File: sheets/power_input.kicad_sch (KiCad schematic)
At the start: 0 parts

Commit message: sch: power input (CH224K PD + 802.3at PoE flyback + 12V OR)
Co-Authored-By: Claude Fable 5 <noreply@anthropic.com>
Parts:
- added BR1, BR2: MB10S, Diode_SMD:D_MBS-4, symbol sierra-to-usb:MB10S
- added C32: 1µF/25V, C_0603, symbol Device:C_Small
- added C_BULK: 68µF/100V, CP_Elec_8x10.5, symbol Device:C_Small
- added C_CLAMP: 0.047µF/250V, C_1206, symbol Device:C_Small
- added C_COMPz: 3.9nF, C_0603, symbol Device:C_Small
- added C_CSF: 100pF, C_0603, symbol Device:C_Small
- added C_GAT2: 0.22µF, C_0603, symbol Device:C_Small
- added C_OUT1: 560µF/25V, CP_Elec_10x10.5, symbol Device:C_Small
- added C_OUT2: 22µF/35V, C_1210, symbol Device:C_Small
- added C_SHIELD: 1nF, C_0603, symbol Device:C_Small
- added C_SST: 47nF, C_0603, symbol Device:C_Small
- added C_VB, C_VBG: 0.1µF, C_0603, symbol Device:C_Small
- added C_VDD: 1µF, C_0603, symbol Device:C_Small
- added D12, D13: MBRS340, Diode_SMD:D_SMC, symbol Device:D_Small
- added D16: MMSD914T1G, D_SOD-123, symbol Device:D_Small
- added D17: MMSZ4685T1G (15V), D_SOD-123, symbol Device:D_Zener_Small
- added D6: SMAJ13A, Diode_SMB:D_SMB, symbol Diode:SMAJ13A
- added D7: SMAJ58A, Diode_SMB:D_SMB, symbol Diode:SMAJ58A
- added D8: BAT54, D_SOD-123, symbol Device:D_Small
- added D9: MMSZ5245B (15V), D_SOD-123, symbol Device:D_Zener_Small
- added J2: TYPE-C-31-M-12, symbol Connector:USB_C_Receptacle_USB2.0_16P
- added L1: 15µH, L_12x12, symbol Device:L
- added L9: 2.2mH, L_0805, symbol Device:L
- added Q20: FDMS86250, Package_TO_SOT_SMD:PQFN-8, symbol Device:Q_NMOS
- added Q21: FDMC2523P, Package_DFN_QFN:QFN-8_2x2mm_P0.5mm, symbol Device:Q_PMOS
- added Q30, Q31: IRLR7843TRPBF, Package_TO_SOT_SMD:TO-252-2, symbol Device:Q_NMOS
- added R41: 2.00kΩ, R_0603, symbol Device:R_Small
- added R45: 40.2kΩ, R_0603, symbol Device:R_Small
- added R53: 10.5kΩ, R_0603, symbol Device:R_Small
- added R_BTPULL, R_GAT2, R_PGPULL, R_VBUSSENSE: 10kΩ, R_0603, symbol Device:R_Small
- added R_CFG1: 24kΩ, R_0603, symbol Device:R_Small
- added R_CLSA, R_CLSB: 32Ω, R_0603, symbol Device:R_Small
- added R_COMPz: 1.00kΩ, R_0603, symbol Device:R_Small
- added R_CS: 0.05Ω, R_2512, symbol Device:R_Small
- added R_CSF, R_VDD: 1kΩ, R_0603, symbol Device:R_Small
- added R_DEN: 25.5kΩ, R_0603, symbol Device:R_Small
- added R_DT: 42.2kΩ, R_0603, symbol Device:R_Small
- added R_FRS: 60.4kΩ, R_0603, symbol Device:R_Small
- added R_G1: 10Ω, R_0603, symbol Device:R_Small
- added R_ISTP: 499kΩ, R_0603, symbol Device:R_Small
- added R_LINEUV_HI: 110kΩ, R_0603, symbol Device:R_Small
- added R_LINEUV_LO: 10.0kΩ, R_0603, symbol Device:R_Small
- added R_REF: 49.9kΩ, R_0603, symbol Device:R_Small
- added R_SHIELD: 1MΩ, R_0603, symbol Device:R_Small
- added T1: WE 750313355, Transformer_SMT_XFRMR_29MM08_23MM1, symbol sierra-to-usb:WE750313355
- added U10: TPS23730RMTR, Package_DFN_QFN:QFN-45-1EP_7x5mm_P0.4mm_EP3.6x3.4mm, symbol sierra-to-usb:TPS23730
- added U19, U21: LM5050MKX-1/NOPB, Package_TO_SOT_SMD:SOT-23-6, symbol sierra-to-usb:LM5050-1
- added U2: CH224K, Package_SO:SSOP-10-1EP_3.9x4.9mm_P1mm_EP2.1x3.3mm, symbol Interface_USB:CH224K
- added U20: TCMT1107, Package_SO:SOP-4_4.4x2.6mm_P1.27mm, symbol Isolator:TCMT1107
- added U22: TL431IDBVR, Package_TO_SOT_SMD:SOT-23-5, symbol Reference_Voltage:TL431DBV
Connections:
- new net +12V: Q30.D, Q31.D, U19.1 (VS), U19.6 (OUT), U21.1 (VS), U21.6 (OUT)
- new net +12V_POE: C_OUT1.1, C_OUT2.1, L1.2, Q31.S, R41.1, R45.1, U21.4 (IN)
- new net +3V3: R_BTPULL.2, R_PGPULL.2
- new net CH224K_CFG1: R_CFG1.1, U2.9 (CFG1)
- new net CH224K_PG: R_PGPULL.1, U2.10 (PG)
- new net CS_SENSE: Q20.S, R_CS.1, R_CSF.1
- new net GND: C_OUT1.2, C_OUT2.2, C_SHIELD.2, C_VDD.2, D13.1 (K), D6.2 (A2), J2.A1 (GND), J2.A12 (GND), J2.B1 (GND), J2.B12 (GND), R53.2, R_CFG1.2, R_SHIELD.2, T1.10 (N2.2), T1.11 (N2.2), T1.12 (N2.2), U19.2 (GND), U19.3 (OFF), U2.11 (GND), U21.2 (GND), U21.3 (OFF), U22.5 (A)
- new net N_ACDRV: C_GAT2.2, D9.2 (A), R_GAT2.1
- new net N_ACLAMP_D: C_CLAMP.1, Q21.D
- new net N_ACLAMP_G: Q21.G, R_GAT2.2
- new net N_BIAS_L_IN: L9.1, T1.5 (N3.1)
- new net N_BIAS_RECT_IN: D16.2 (A), L9.2
- new net N_CH224K_VBUSSENSE: R_VBUSSENSE.2, U2.8 (VBUS)
- new net N_CH224K_VDD: C_VDD.1, R_VDD.2, U2.1 (VDD)
- new net N_FBTAP: R45.2, R53.1, U22.4 (REF)
- new net N_G1: D8.2 (A), Q20.G, R_G1.2
- new net N_GAT2: C_GAT2.1, U10.41 (GAT2)
- new net N_GATE: D8.1 (K), R_G1.1, U10.43 (GATE)
- new net N_J2_SHIELD: C_SHIELD.1, J2.SH (SHIELD), R_SHIELD.1
- new net N_LED_A: R41.2, U20.1
- new net N_OPTO_E: R_COMPz.1, U20.3
- new net N_SEC_PLUS: D12.1 (K), T1.7 (N2.1), T1.8 (N2.1), T1.9 (N2.1)
- new net N_TL_K: U20.2, U22.3 (K)
- new net N_U10_CLSA: R_CLSA.1, U10.21 (CLSA)
- new net N_U10_CLSB: R_CLSB.1, U10.20 (CLSB)
- new net N_U10_COMP: C_COMPz.1, R_COMPz.2, U10.35 (COMP)
- new net N_U10_CS: C_CSF.1, R_CSF.2, U10.1 (CS)
- new net N_U10_DEN: R_DEN.1, U10.24 (DEN)
- new net N_U10_DT: R_DT.1, U10.31 (DT)
- new net N_U10_FRS: R_FRS.1, U10.4 (FRS)
- new net N_U10_ISTP: R_ISTP.1, U10.32 (I_STP)
- new net N_U10_LINEUV: R_LINEUV_HI.2, R_LINEUV_LO.1, U10.38 (LINEUV)
- new net N_U10_REF: R_REF.1, U10.17 (REF)
- new net N_U10_SST: C_SST.1, U10.33 (SST)
- new net N_U10_VB: C_VB.1, U10.3 (DTHR), U10.34 (FB), U10.37 (VB), U20.4
- new net N_U10_VBG: C_VBG.1, U10.40 (VBG)
- new net N_U10_VCC: C32.1, D16.1 (K), D17.1 (K), U10.42 (VCC)
- new net N_U19_GATE: Q30.G, U19.5 (GATE)
- new net N_U21_GATE: Q31.G, U21.5 (GATE)
- new net PD_CC1: J2.A5 (CC1), U2.7 (CC1)
- new net PD_CC2: J2.B5 (CC2), U2.6 (CC2)
- new net POE_RTN: BR1.3 (-), BR2.3 (-), C32.2, C_BULK.2, C_COMPz.2, C_CSF.2, C_SST.2, C_VB.2, C_VBG.2, D17.2 (A), D7.2 (A2), R_CLSA.2, R_CLSB.2, R_CS.2, R_DT.2, R_FRS.2, R_ISTP.2, R_LINEUV_LO.2, R_REF.2, T1.6 (N3.2), U10.11 (EMPS), U10.18 (SCDIS), U10.19 (PPD), U10.2 (AGND), U10.27 (VSS1), U10.28 (VSS2), U10.39 (PSRS), U10.44 (CP), U10.45 (GND), U10.46 (PAD_G), U10.47 (PAD_S), U10.5 (APD), U10.7 (RTN1), U10.8 (RTN2), U10.9 (RTN3)
- new net POE_STATUS: R_BTPULL.1, U10.12 (BT)
- new net POE_VA+: BR1.2
- new net POE_VA-: BR1.4
- new net POE_VB+: BR2.2
- new net POE_VB-: BR2.4
- new net POE_VDD54: BR1.1 (+), BR2.1 (+), C_BULK.1, D7.1 (A1), D9.1 (K), Q21.S, R_DEN.2, R_LINEUV_HI.1, T1.1 (N1.1), T1.2 (N1.1), U10.23 (VDD)
- new net SW2: D12.2 (A), D13.2 (A), L1.1
- new net SW_NODE: C_CLAMP.2, Q20.D, T1.3 (N1.2), T1.4 (N1.2)
- new net VBUS_PD: D6.1 (A1), J2.A4 (VBUS), J2.A9 (VBUS), J2.B4 (VBUS), J2.B9 (VBUS), Q30.S, R_VBUSSENSE.1, R_VDD.1, U19.4 (IN)
- no-connect marks 0 -> 22

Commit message: sch: power_input rework — faithful EVM-093 transcription, VSS/RTN split, sync rect, opto/comp per EVM
Co-Authored-By: Claude Fable 5 <noreply@anthropic.com>
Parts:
- removed C_BULK: 68µF/100V, CP_Elec_8x10.5, symbol Device:C_Small
- removed C_CLAMP: 0.047µF/250V, C_1206, symbol Device:C_Small
- removed C_COMPz: 3.9nF, C_0603, symbol Device:C_Small
- removed C_CSF: 100pF, C_0603, symbol Device:C_Small
- removed C_GAT2: 0.22µF, C_0603, symbol Device:C_Small
- removed C_OUT1: 560µF/25V, CP_Elec_10x10.5, symbol Device:C_Small
- removed C_OUT2: 22µF/35V, C_1210, symbol Device:C_Small
- removed C_SHIELD: 1nF, C_0603, symbol Device:C_Small
- removed C_SST: 47nF, C_0603, symbol Device:C_Small
- removed C_VB, C_VBG: 0.1µF, C_0603, symbol Device:C_Small
- removed C_VDD: 1µF, C_0603, symbol Device:C_Small
- removed D16: MMSD914T1G, D_SOD-123, symbol Device:D_Small
- removed D17: MMSZ4685T1G (15V), D_SOD-123, symbol Device:D_Zener_Small
- removed D6: SMAJ13A, Diode_SMB:D_SMB, symbol Diode:SMAJ13A
- removed D7: SMAJ58A, Diode_SMB:D_SMB, symbol Diode:SMAJ58A
- removed L9: 2.2mH, L_0805, symbol Device:L
- removed R41: 2.00kΩ, R_0603, symbol Device:R_Small
- removed R45: 40.2kΩ, R_0603, symbol Device:R_Small
- removed R53: 10.5kΩ, R_0603, symbol Device:R_Small
- removed R_BTPULL, R_GAT2, R_PGPULL, R_VBUSSENSE: 10kΩ, R_0603, symbol Device:R_Small
- removed R_CFG1: 24kΩ, R_0603, symbol Device:R_Small
- removed R_CLSA, R_CLSB: 32Ω, R_0603, symbol Device:R_Small
- removed R_COMPz: 1.00kΩ, R_0603, symbol Device:R_Small
- removed R_CS: 0.05Ω, R_2512, symbol Device:R_Small
- removed R_CSF, R_VDD: 1kΩ, R_0603, symbol Device:R_Small
- removed R_DEN: 25.5kΩ, R_0603, symbol Device:R_Small
- removed R_DT: 42.2kΩ, R_0603, symbol Device:R_Small
- removed R_FRS: 60.4kΩ, R_0603, symbol Device:R_Small
- removed R_G1: 10Ω, R_0603, symbol Device:R_Small
- removed R_ISTP: 499kΩ, R_0603, symbol Device:R_Small
- removed R_LINEUV_HI: 110kΩ, R_0603, symbol Device:R_Small
- removed R_LINEUV_LO: 10.0kΩ, R_0603, symbol Device:R_Small
- removed R_REF: 49.9kΩ, R_0603, symbol Device:R_Small
- removed R_SHIELD: 1MΩ, R_0603, symbol Device:R_Small
- added C1: 1uF, C_0603, symbol Device:C_Small
- added C10: 470pF/100V, C_0805, symbol Device:C_Small
- added C11: 2.2nF/50V, C_0603, symbol Device:C_Small
- added C12: 47nF/50V, C_0603, symbol Device:C_Small
- added C13, C14: 0.1uF/25V, C_0603, symbol Device:C_Small
- added C15: 0.1uF/50V, C_0805, symbol Device:C_Small
- added C16: 1uF/25V, C_0805, symbol Device:C_Small
- added C17: 0.047uF/250V, C_1206, symbol Device:C_Small
- added C18: 0.22uF/50V, C_0805, symbol Device:C_Small
- added C19: 2200pF/2kV, C_1808, symbol Device:C_Small
- added C2: 1nF, C_0603, symbol Device:C_Small
- added C20: 1nF/100V, C_0603, symbol Device:C_Small
- added C21, C23: 0.047uF/100V, C_1206, symbol Device:C_Small
- added C22, C31: 100pF/25V, C_0603, symbol Device:C_Small
- added C24: 1000pF/100V, C_1206, symbol Device:C_Small
- added C25: 39uF/16V, CP_Elec_6.3x5.8, symbol Device:C_Small
- added C26, C27: 22uF/35V, C_1210, symbol Device:C_Small
- added C28: 560uF/25V, CP_Elec_10x10.5, symbol Device:C_Small
- added C29: 68nF/16V, C_0603, symbol Device:C_Small
- added C3, C9: 0.1uF/100V, C_1206, symbol Device:C_Small
- added C30: 1uF/50V, C_0805, symbol Device:C_Small
- added C4: 68uF/100V, CP_Elec_10x13, symbol Device:C_Small
- added C5, C6, C7: 2.2uF/100V, C_1210, symbol Device:C_Small
- added C8: 0.1uF/100V, C_0805, symbol Device:C_Small
- added D1, D2, D3, D4, D5: MMSD914T1G, D_SOD-123, symbol Device:D_Small
- added D14: MMSZ5242B-7-F 12V, D_SOD-123, symbol Device:D_Zener_Small
- added D15: BAT54S-7-F, Package_TO_SOT_SMD:SOT-23, symbol Diode:BAT54S
- added D16: Yellow 0603, LED_0603, symbol Device:LED
- added D6: SMAJ13A, Diode_SMB:D_SMB, symbol sierra-to-usb:SMAJ13A
- added D7: SMAJ58A, Diode_SMB:D_SMB, symbol sierra-to-usb:SMAJ58A
- added L2: 5.5uH, L_WE-HC6, symbol Device:L
- added L3: 2.2mH, L_7x7, symbol Device:L
- added Q22, Q23: BSC057N08NS3 G, Package_TO_SOT_SMD:PG-TDSON-8, symbol Device:Q_NMOS
- added Q24, Q25: FCX493TA, Package_TO_SOT_SMD:SOT-89-3, symbol Device:Q_NPN
- added R1: 1k, R_0603, symbol Device:R_Small
- added R10: 110k, R_0603, symbol Device:R_Small
- added R11, R18, R33, R37, R38: 10.0k, R_0603, symbol Device:R_Small
- added R12: 237k, R_0603, symbol Device:R_Small
- added R13: 60.4k, R_0603, symbol Device:R_Small
- added R14: 49.9k, R_0603, symbol Device:R_Small
- added R15: 42.2k, R_0603, symbol Device:R_Small
- added R16: 499k, R_0603, symbol Device:R_Small
- added R17: 10.0, R_0603, symbol Device:R_Small
- added R19: 3.00k, R_0603, symbol Device:R_Small
- added R2, R4: 10k, R_0603, symbol Device:R_Small
- added R20: 0.05/1W, R_1206, symbol Device:R_Small
- added R21: 4.02k, R_1206, symbol Device:R_Small
- added R22: 8.06k, R_1206, symbol Device:R_Small
- added R23: 2.0k, R_0603, symbol Device:R_Small
- added R24: 5.10, R_0805, symbol Device:R_Small
- added R25, R26: 10k/1W, R_2512, symbol Device:R_Small
- added R27: 100/1W, R_2512, symbol Device:R_Small
- added R28: 49.9, R_0603, symbol Device:R_Small
- added R29: 40.2k, R_0603, symbol Device:R_Small
- added R3: 24k, R_0603, symbol Device:R_Small
- added R30: 10.5k, R_0603, symbol Device:R_Small
- added R31, R32, R35: 2.00k, R_0603, symbol Device:R_Small
- added R34, R36: 1.00k, R_0603, symbol Device:R_Small
- added R5: 1M, R_0603, symbol Device:R_Small
- added R6: 25.5k, R_0603, symbol Device:R_Small
- added R7, R8: 32, R_0805, symbol Device:R_Small
- added R9: 15.0k, R_0603, symbol Device:R_Small
- added U23: FOD817DS, Package_DIP:DIP-4_W7.62mm_SMDGullWing, symbol Isolator:PC817
- C32: value 1µF/25V -> 3.9nF/50V
- D12, D13: value MBRS340 -> MURA110T3G; footprint Diode_SMD:D_SMC -> D_SMA
- D8: value BAT54 -> MMSD914T1G
- D9: value MMSZ5245B (15V) -> MMSZ5242B-7-F 12V
- L1: value 15µH -> 15uH; footprint L_12x12 -> L_18x18
- Q20: footprint Package_TO_SOT_SMD:PQFN-8 -> Package_DFN_QFN:PQFN08A
- Q21: footprint Package_DFN_QFN:QFN-8_2x2mm_P0.5mm -> Package_DFN_QFN:QFN-8_2x2mm
- T1: value WE 750313355 -> 750313355
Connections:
- net N_ACDRV is gone; now on net GND: D9.2 (A)
- net N_OPTO_E is gone; now on net POE_RTN: U20.3
- net +12V_POE: now also C25.1, C26.1, C27.1, C28.1, D16.2 (A), R28.1
- net +3V3: now also R4.2
- net CH224K_CFG1: now also R3.1
- net CH224K_PG: now also R4.1
- net GND: now also C1.2, C19.2, C2.2, C20.2, C21.2, C23.2, C25.2, C26.2, C27.2, C28.2, C30.2, D14.2 (A), D6.2 (A), Q22.S, Q23.S, R22.2, R25.2, R26.2, R27.2, R3.2, R30.2, R5.2, U23.3; no longer D13.1 (K), T1.10 (N2.2), T1.11 (N2.2), T1.12 (N2.2)
- net N_CH224K_VBUSSENSE: now also R2.2
- net N_CH224K_VDD: now also C1.1, R1.2
- net N_GAT2: now also C18.1
- net N_GATE: now also D4.1 (K), R17.1; no longer D8.1 (K)
- net N_J2_SHIELD: now also C2.1, R5.1
- net POE_RTN: now also Q21.S, C11.2, C12.2, C13.2, C14.2, C15.2, C16.2, C19.1, C3.2, C4.2, C5.2, C6.2, C7.2, C8.2, D2.2 (A), D3.2 (A), R11.2, R13.2, R15.2, R16.2, R18.2, R20.2; no longer BR1.3 (-), BR2.3 (-), C32.2, U10.11 (EMPS), U10.18 (SCDIS), U10.19 (PPD), U10.27 (VSS1), U10.28 (VSS2), U10.44 (CP), U10.47 (PAD_S)
- net POE_VDD54: now also C3.1, C4.1, D7.1 (K), L2.1, R10.1, R6.2; no longer D9.1 (K), Q21.S, T1.1 (N1.1), T1.2 (N1.1), U10.23 (VDD)
- net VBUS_PD: now also D6.1 (K), R1.1, R2.1
- net CS_SENSE renamed N_CS_SNS
- net N_CS_SNS: now also R19.2, R20.1
- net N_ACLAMP_D renamed N_CLAMP_D
- net N_CLAMP_D: now also C17.2
- net N_ACLAMP_G renamed N_CLAMP_G
- net N_CLAMP_G: now also C18.2, D3.1 (K), R18.1
- net N_BIAS_L_IN renamed N_AUX
- net N_AUX: now also D1.2 (A)
- net N_FBTAP renamed N_FBREF
- net N_FBREF: now also C32.2, C31.2, R29.2, R30.1
- net N_G1 renamed N_GATE_Q
- net N_GATE_Q: now also D4.2 (A), R17.2; no longer D8.2 (A)
- net N_LED_A renamed N_LEDA
- net N_LEDA: now also R31.2
- net N_SEC_PLUS renamed N_SEC_SW
- net N_SEC_SW: now also D12.2 (A), L1.1, C24.1, D5.1 (K), Q23.D, Q24.C, R21.1; no longer D12.1 (K)
- net N_TL_K renamed N_TLK
- net N_TLK: now also C31.1, D15.1 (A), R32.2, R34.1
- net N_U10_CLSA renamed N_CLSA
- net N_CLSA: now also R7.1
- net N_U10_CLSB renamed N_CLSB
- net N_CLSB: now also R8.1
- net N_U10_COMP renamed N_COMP
- net N_COMP: now also U20.4, C29.2, R35.2
- net N_U10_CS renamed N_CS
- net N_CS: now also R19.1
- net N_U10_DEN renamed N_DEN
- net N_DEN: now also R6.1
- net N_U10_DT renamed N_DT
- net N_DT: now also R15.1
- net N_U10_FRS renamed N_FRS
- net N_FRS: now also R12.2, R13.1
- net N_U10_ISTP renamed N_ISTP
- net N_ISTP: now also R16.1
- net N_U10_LINEUV renamed N_LINEUV
- net N_LINEUV: now also R10.2, R11.1
- net N_U10_REF renamed N_REF
- net N_REF: now also R14.1
- net N_U10_SST renamed N_SST
- net N_SST: now also C12.1
- net N_U10_VB renamed N_VB
- net N_VB: now also C13.1, R35.1, R36.1, R37.1; no longer U10.3 (DTHR), U20.4
- net N_U10_VBG renamed N_VBG
- net N_VBG: now also C14.1
- net N_U10_VCC renamed N_C32Z
- net N_C32Z: now also R34.2; no longer U10.42 (VCC)
- net POE_STATUS renamed N_BT
- net N_BT: now also U23.2
- removed net SW2: D12.2 (A), D13.2 (A), L1.1
- net SW_NODE renamed N_SW
- net N_SW: now also C17.1
- new net N_AUX_R: D1.1 (K), D2.1 (K), L3.1
- new net N_BTLED: R37.2, U23.1
- new net N_BTLED2: D16.1 (K), R38.1
- new net N_BTSTAT: R38.2, U23.4
- new net N_D15COM: C30.1, D15.3 (COM), R33.2
- new net N_DTHR: C11.1, R12.1, U10.3 (DTHR)
- new net N_FBTOP: D15.2 (K), R28.2, R29.1, R31.1, R32.1, R33.1
- new net N_PPD: C10.1, R9.1, U10.19 (PPD)
- new net N_Q22_G: D5.2 (A), Q22.G, Q24.E
- new net N_Q22_RC: C20.1, R24.2
- new net N_Q22_RCD: C21.1, D13.1 (K), R25.1
- new net N_Q23_G: D8.2 (A), Q23.G, Q25.E
- new net N_Q24_B: D9.1 (K), Q24.B, R21.2, R22.1
- new net N_Q25_B: C22.2, D14.1 (K), Q25.B, R23.2
- new net N_R43C44: C29.1, R36.2
- new net N_SEC_CLP: C23.1, D12.1 (K), R26.1
- new net N_SEC_RC: C24.2, R27.1
- new net N_SEC_RTN: C22.1, D13.2 (A), D8.1 (K), Q22.D, Q25.C, R23.1, R24.1, T1.10 (N2.2), T1.11 (N2.2), T1.12 (N2.2)
- new net N_VCC: C15.1, C16.1, L3.2, U10.42 (VCC)
- new net POE_VDD54_F: C5.1, C6.1, C7.1, C8.1, C9.1, L2.2, T1.1 (N1.1), T1.2 (N1.1), U10.23 (VDD)
- new net POE_VSS: BR1.3 (-), BR2.3 (-), C10.2, C9.2, D7.2 (A), R14.2, R7.2, R8.2, R9.2, U10.27 (VSS), U10.28 (VSS), U10.47 (PAD_S)
- no-connect marks 22 -> 25
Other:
- note added: "Isolation: T1, U20, U23 and Y-cap C19 (2kV) are the only barrier-crossing components. Primary domain: POE_VDD54/POE_VDD54_F/POE_VSS/POE_RTN. Secondary: GND/+12V_POE."
- note added: "TODO(mcu): POE_STATUS net dropped on this sheet — EVM-093 exposes BT only as an isolated LED indicator (U23 opto, D16/R38 from +12V_POE). Node N_BTSTAT swings ~0-11V, NOT 3V3-safe. Re-plan the MCU status input (e.g. repurpose U23 collector with a +3V3 pull-up in place of the D16/R38 LED chain) before wiring the mcu sheet."

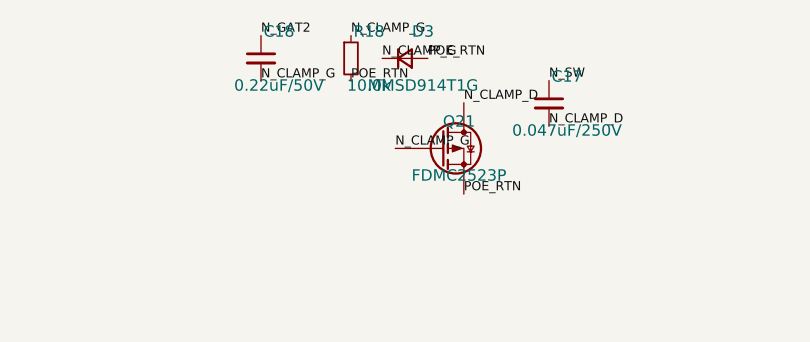
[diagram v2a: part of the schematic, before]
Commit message: sch: power_input — fix D3 clamp DC-restore orientation per EVM D20
Co-Authored-By: Claude Fable 5 <noreply@anthropic.com>
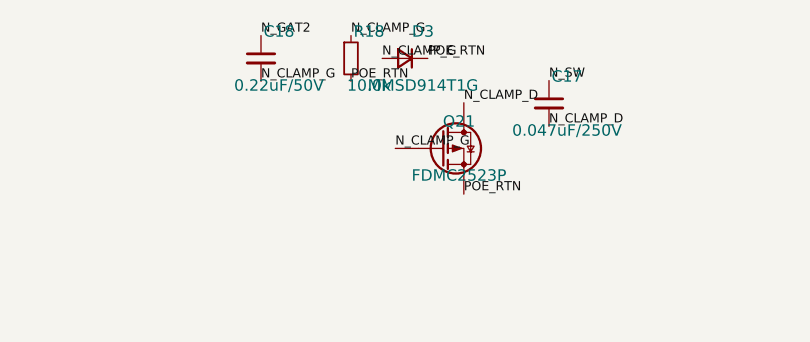
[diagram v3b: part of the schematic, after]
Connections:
- net N_CLAMP_G: now also D3.2 (A); no longer D3.1 (K)
- net POE_RTN: now also D3.1 (K); no longer D3.2 (A)
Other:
- moved on the sheet: D3
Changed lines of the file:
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@@
 	(symbol
 		(lib_id "Device:D_Small")
-		(at 346 15 0)
+		(at 346 15 180)
 		(unit 1)
 		(exclude_from_sim no)

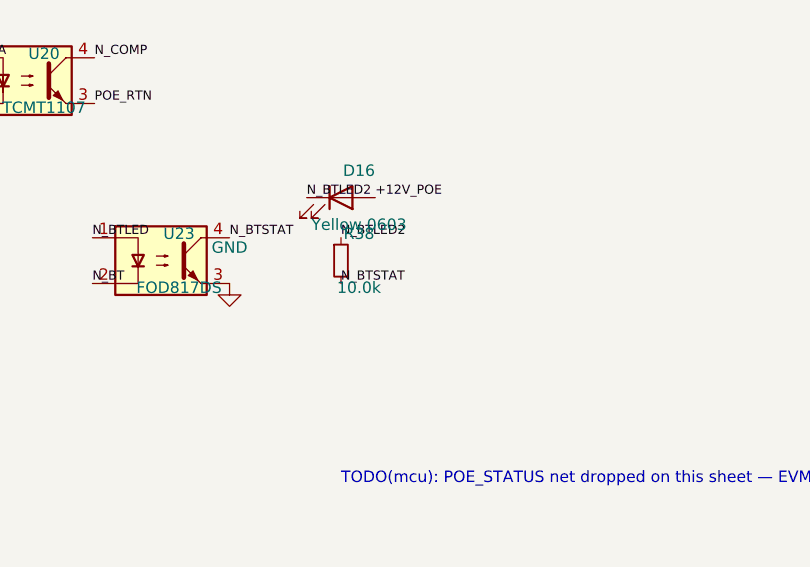
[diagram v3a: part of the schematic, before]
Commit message: sch: RP2040 control plane + GPIO map
RP2040 (U24) core: W25Q128JVS QSPI flash, 12MHz crystal, RUN/BOOTSEL,
USB debug PHY (27.4R series), SWD, full 30-pin GPIO map per spec Sec.7.2.
I2C bus (2x TMP112 + Qwiic) pulled to +3V3_MCU, not +3V3, so an unpowered
RP2040 domain can't be back-fed through its own (non-failsafe) GPIOs.
LED-kill reworked high-side (Q33 DMG3415U-7 P-FET): SW2 slide switch and
GP9/LED_EN_CTL are independent kills, resistor values chosen so SW2 always
wins even if firmware fights it. RGB (SK6805-EC15, new custom symbol) runs
off the killable LED_PWR rail. POE_STS_RAW global label added to
power_input.kicad_sch (N_BTSTAT node) + divider on this sheet; GPIO
binding is BLOCKED (brief's GP0-29 map has no free slot) and left
unconnected pending a human decision -- see task-9-report.md.

0 errors / 600 ERC warnings (was 512), all checks pass.

Co-Authored-By: Claude Fable 5 <noreply@anthropic.com>
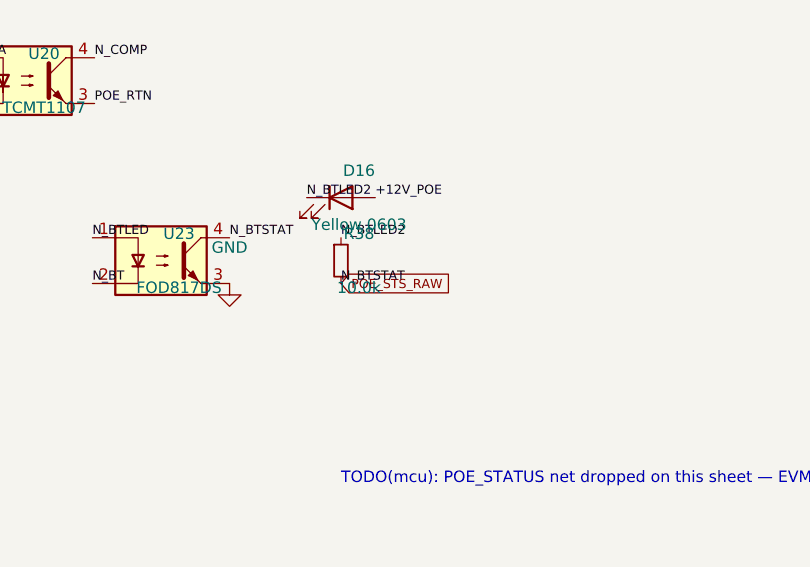
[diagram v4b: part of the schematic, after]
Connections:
- net N_BTSTAT renamed POE_STS_RAW
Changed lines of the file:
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@@
 		(effects (font (size 1.016 1.016)) (justify left bottom))
+	)
+	(global_label "POE_STS_RAW"
+		(shape input)
+		(at 540.0 152.54 0)
+		(effects (font (size 1.016 1.016)) (justify left bottom))
+		(property "Intersheetrefs" "${INTERSHEET_REFS}" (at 540.0 152.54 0) (effects (font (size 1.27 1.27))))
 	)
 	(symbol
